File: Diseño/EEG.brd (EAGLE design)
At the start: 49.8 x 80 mm, 42 parts, among them IC1 REF2033AIDDCT, IC2 MCP73831T-2ACI_OT, IC3 LP38692MP-3.3_NOPB, J1 USB3500-30-A-KIT, J2 SJ3-35083A-TR, J3 1769

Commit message: añadido valores cap de carga
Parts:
- C1, C2: value (none) -> 10u
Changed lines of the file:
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@@
 <attribute name="VALUE" x="13.0175" y="34.6075" size="1.27" layer="27" rot="R180" align="center"/>
 </element>
-<element name="C1" library="rcl" library_urn="urn:adsk.eagle:library:334" package="C0805K" package3d_urn="urn:adsk.eagle:package:23681/2" value="" x="22.86" y="22.86" smashed="yes" rot="R180">
+<element name="C1" library="rcl" library_urn="urn:adsk.eagle:library:334" package="C0805K" package3d_urn="urn:adsk.eagle:package:23681/2" value="10u" x="22.86" y="22.86" smashed="yes" rot="R180">
 <attribute name="NAME" x="22.01875" y="20.8775" size="1.016" layer="25"/>
 <attribute name="POPULARITY" value="52" x="-25.4" y="93.98" size="1.778" layer="27" rot="R180" display="off"/>
@@
 <attribute name="VALUE" x="36.195" y="26.67" size="1.27" layer="27" rot="R90"/>
 </element>
-<element name="C2" library="rcl" library_urn="urn:adsk.eagle:library:334" package="C0805K" package3d_urn="urn:adsk.eagle:package:23681/2" value="" x="27.94" y="22.86" smashed="yes">
+<element name="C2" library="rcl" library_urn="urn:adsk.eagle:library:334" package="C0805K" package3d_urn="urn:adsk.eagle:package:23681/2" value="10u" x="27.94" y="22.86" smashed="yes">
 <attribute name="NAME" x="27.09875" y="20.8775" size="1.016" layer="25"/>
 <attribute name="POPULARITY" value="52" x="80.01" y="-48.26" size="1.778" layer="27" display="off"/>

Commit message: Correcciones del profesor
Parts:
- C1, C2: value 10u -> (none)
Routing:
- net +5V: track 72.0 -> 73.4 mm
- net O1: track 51.2 -> 52.5 mm
- net N$10: track 19.8 -> 18.9 mm
- net VSS: track 119.3 -> 120.3 mm
- net CS1: track 27.8 -> 27.2 mm
- net N$15: track 27.6 -> 28.2 mm

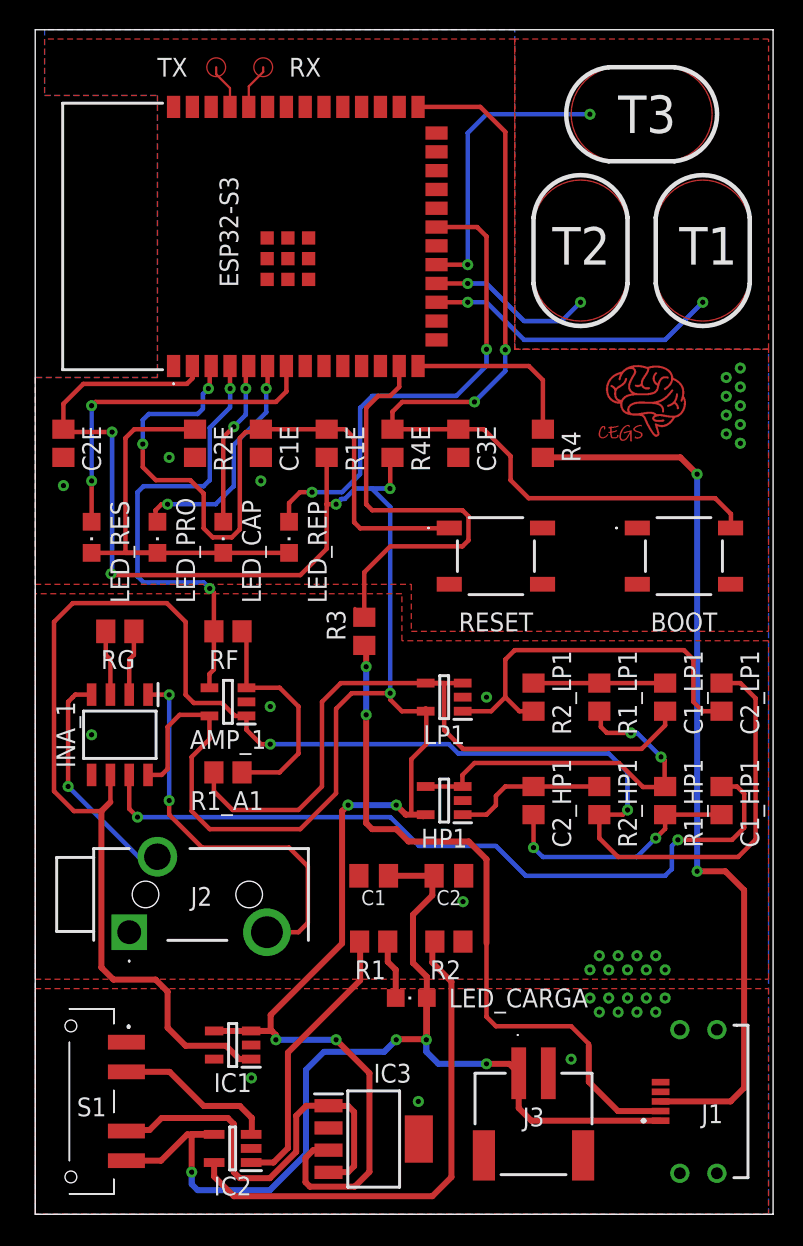
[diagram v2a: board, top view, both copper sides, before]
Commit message: añadido oled, componentes nuevos, restio de leds y correcion de pistas
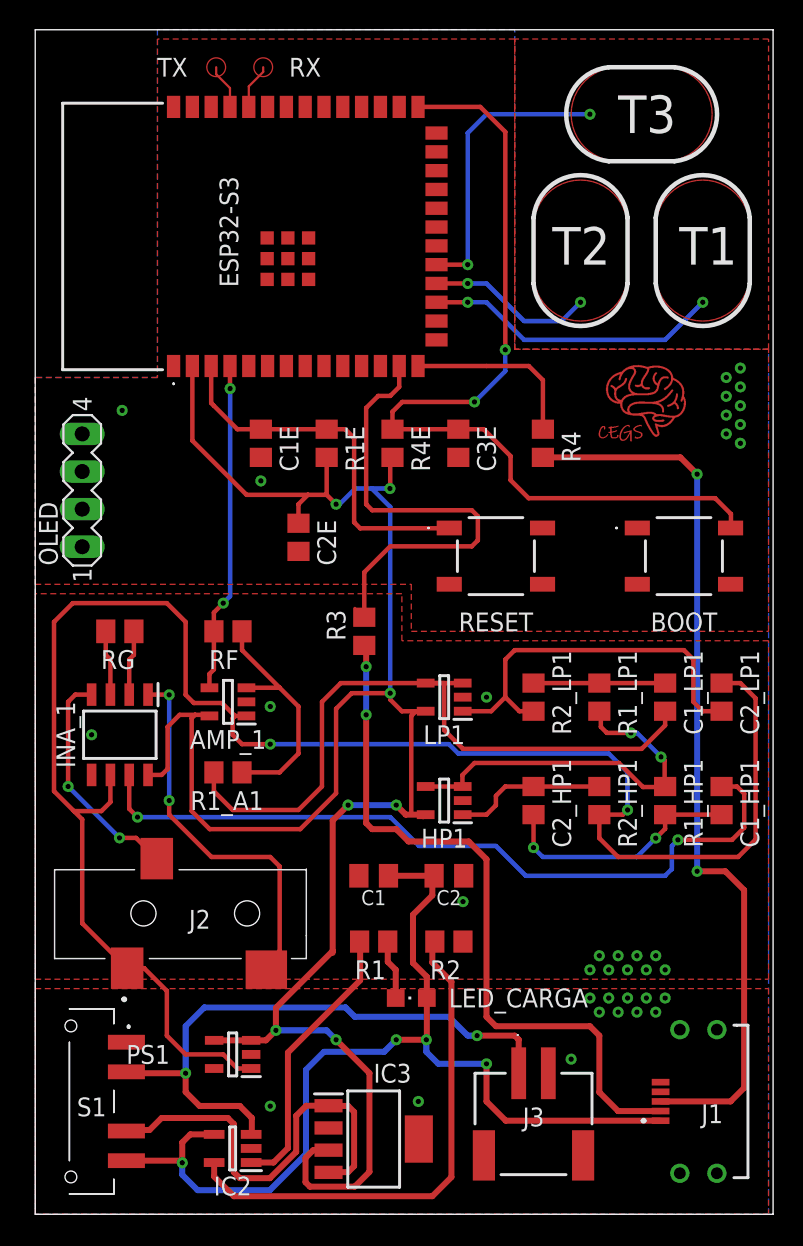
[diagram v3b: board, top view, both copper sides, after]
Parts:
- removed IC1: REF2033AIDDCT, REF2033AIDDCT:SOT95P280X110-5N
- removed LED_CAP, LED_PRO, LED_REP, LED_RES: (no value), led:CHIPLED_0805
- removed R2E: 220, rcl:R0805
- added OLED: (no value), con-lstb:MA04-1
- added PS1: REF2033AIDDCR, REF2033AIDDCR:SOT95P280X110-5N
- J2: value SJ3-35083A-TR -> SJ-3523-SMT-TR; device SJ3-35083A-TR:SJ335083ATR -> SJ-3523-SMT-TR:SJ3523SMTTR
- moved C2E 17.1 mm to (17.8, 45.7)
- moved J2 2.84 mm to (3.81, 20.3)
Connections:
- removed net +5V1: ESP32-S3.22
- removed net LED_REP: ESP32-S3.21, LED_REP.A
- removed net N$1: ESP32-S3.5, LED_CAP.A
- removed net N$15: LED_CAP.C, LED_PRO.C, LED_REP.C, LED_RES.C, R2E.2
- removed net N$16: ESP32-S3.6, LED_PRO.A
- removed net N$17: ESP32-S3.7, LED_RES.A
- new net SCL: ESP32-S3.38, OLED.3
- new net SDA: ESP32-S3.34, OLED.4
- net +3V3: now also OLED.2, PS1.3, PS1.4; no longer IC1.3, IC1.4
- net +5V: no longer J3.1
- net +BATT: now also J3.1
- net CS2: now also J2.3; no longer J2.5
- net GND: now also OLED.1, PS1.2; no longer IC1.2, J2.1, R2E.1
- net VSS: now also J2.1, PS1.1; no longer IC1.1
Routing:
- net LED_REP: track 33.5 -> 0.00 mm, vias 2 -> 0
- net +BATT: track 10.9 -> 41.0 mm, vias 0 -> 2
- net N$15: track 28.2 -> 0.00 mm
- net +3V3: track 167.3 -> 139.4 mm, vias 9 -> 7
- net N$17: track 23.8 -> 0.00 mm, vias 2 -> 0
- net N$19: track 47.5 -> 25.7 mm, vias 2 -> 0
- net N$16: track 16.4 -> 0.00 mm, vias 2 -> 0
- net N$1: track 11.2 -> 0.00 mm, vias 2 -> 0
- net O4: track 32.0 -> 23.0 mm
- net +5V: track 73.4 -> 68.1 mm
- net VSS: track 120.3 -> 121.8 mm
- net CS1: track 27.2 -> 25.8 mm
- net N$18: track 31.5 -> 32.7 mm
- net N$8: track 15.5 -> 16.4 mm
- net USB_2: track 47.8 -> 48.5 mm
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
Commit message: añadí las rutas del nuevo componente
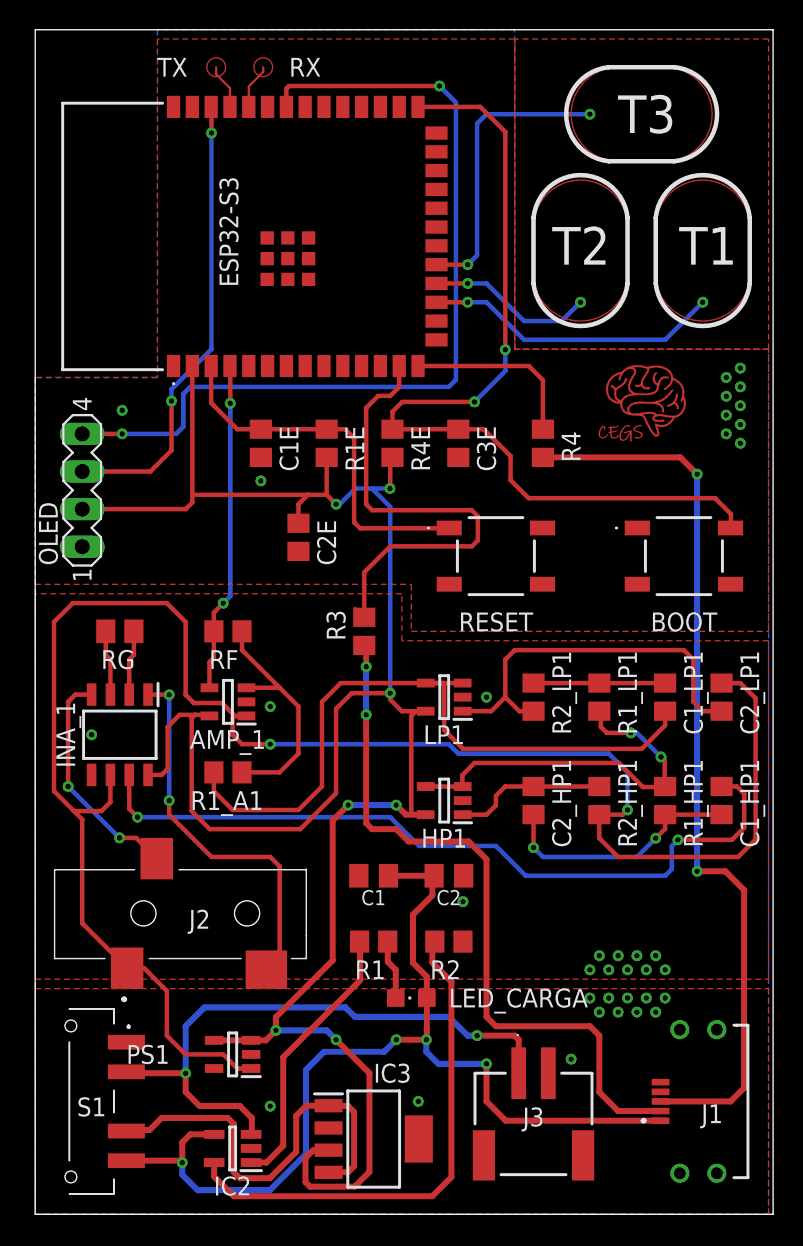
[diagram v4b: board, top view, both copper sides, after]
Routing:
- net SDA: track 0.00 -> 60.0 mm, vias 0 -> 2
- net SCL: track 0.00 -> 30.9 mm, vias 0 -> 2
- net +3V3: track 139.4 -> 149.6 mm
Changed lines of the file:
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@@
 <wire x1="20.32" y1="11.7856" x2="22.57425" y2="9.53135" width="0.4064" layer="1"/>
 <wire x1="22.57425" y1="9.53135" x2="22.57425" y2="2.86098125" width="0.4064" layer="1"/>
-<wire x1="20.0914" y1="17.653" x2="20.0914" y2="17.78" width="0.4064" layer="1"/>
-<wire x1="20.0914" y1="17.78" x2="20.0914" y2="26.5938" width="0.4064" layer="1"/>
+<wire x1="20.0914" y1="17.145" x2="20.0914" y2="26.5938" width="0.4064" layer="1"/>
 <wire x1="20.0914" y1="26.5938" x2="21.1328" y2="27.6352" width="0.4064" layer="1"/>
 <via x="21.1328" y="27.6352" extent="1-16" drill="0.35"/>
@@
 <contactref element="PS1" pad="4"/>
 <wire x1="12.085" y1="11.745" x2="14.585" y2="11.745" width="0.4064" layer="1"/>
-<wire x1="16.256" y1="13.9446" x2="16.256" y2="12.4206" width="0.4064" layer="1"/>
-<wire x1="20.0914" y1="17.78" x2="16.256" y2="13.9446" width="0.4064" layer="1"/>
+<wire x1="16.256" y1="13.3096" x2="16.256" y2="12.4206" width="0.4064" layer="1"/>
+<wire x1="20.0914" y1="17.145" x2="16.256" y2="13.3096" width="0.4064" layer="1"/>
 <wire x1="14.585" y1="11.745" x2="15.5804" y2="11.745" width="0.4064" layer="1"/>
 <wire x1="15.5804" y1="11.745" x2="16.256" y2="12.4206" width="0.4064" layer="1"/>
 <wire x1="19.685" y1="48.5902" x2="20.32" y2="47.9552" width="0.3048" layer="1"/>
-<wire x1="10.615" y1="57.29" x2="10.615" y2="52.25" width="0.3048" layer="1"/>
-<wire x1="14.2748" y1="48.5902" x2="18.415" y2="48.5902" width="0.3048" layer="1"/>
+<wire x1="10.615" y1="57.29" x2="10.615" y2="48.5775" width="0.3048" layer="1"/>
+<wire x1="10.615" y1="48.5775" x2="10.615" y2="48.08" width="0.3048" layer="1"/>
 <wire x1="18.415" y1="48.5902" x2="19.685" y2="48.5902" width="0.3048" layer="1"/>
-<wire x1="10.615" y1="52.25" x2="14.2748" y2="48.5902" width="0.3048" layer="1"/>
 <wire x1="25.4" y1="33.655" x2="25.7175" y2="33.9725" width="0.3048" layer="1"/>
 <wire x1="25.7175" y1="33.9725" x2="25.72" y2="33.975" width="0.3048" layer="1"/>
@@
 <wire x1="17.78" y1="46.67" x2="17.78" y2="47.9552" width="0.3048" layer="1"/>
 <wire x1="17.78" y1="47.9552" x2="18.415" y2="48.5902" width="0.3048" layer="1"/>
-<wire x1="10.795" y1="57.11" x2="3.175" y2="47.625" width="0" layer="19" extent="1-1"/>
+<wire x1="3.175" y1="47.625" x2="10.16" y2="47.625" width="0.3048" layer="1"/>
+<wire x1="10.16" y1="47.625" x2="10.615" y2="48.08" width="0.3048" layer="1"/>
+<wire x1="10.6277" y1="48.5902" x2="10.615" y2="48.5775" width="0.3048" layer="1"/>
+<wire x1="18.415" y1="48.5902" x2="10.6277" y2="48.5902" width="0.3048" layer="1"/>
 </signal>
 <signal name="GND">
@@
 <contactref element="R1" pad="1"/>
 <wire x1="14.585" y1="3.495" x2="14.605" y2="3.475" width="0.1524" layer="1"/>
-<wire x1="14.585" y1="3.495" x2="16.0934" y2="3.495" width="0.4064" layer="1"/>
-<wire x1="17.0688" y1="4.4704" x2="17.0688" y2="10.922" width="0.4064" layer="1"/>
-<wire x1="17.0688" y1="10.922" x2="21.9456" y2="15.7988" width="0.4064" layer="1"/>
+<wire x1="14.585" y1="3.495" x2="15.61715" y2="3.495" width="0.4064" layer="1"/>
+<wire x1="16.7513" y1="4.62915" x2="16.7513" y2="10.6045" width="0.4064" layer="1"/>
+<wire x1="16.7513" y1="10.6045" x2="21.9456" y2="15.7988" width="0.4064" layer="1"/>
 <wire x1="21.9456" y1="15.7988" x2="21.9456" y2="18.3794" width="0.4064" layer="1"/>
 <wire x1="21.9456" y1="18.3794" x2="21.91" y2="18.415" width="0.4064" layer="1"/>
-<wire x1="16.0934" y1="3.495" x2="17.0688" y2="4.4704" width="0.4064" layer="1"/>
+<wire x1="15.61715" y1="3.495" x2="16.7513" y2="4.62915" width="0.4064" layer="1"/>
 </signal>
 <signal name="N$2">
@@
 <contactref element="RF" pad="2"/>
 <contactref element="ESP32-S3" pad="4"/>
-<wire x1="11.7675" y1="36.4925" x2="11.7675" y2="35.5575" width="0.3048" layer="1"/>
-<wire x1="12.0675" y1="36.7925" x2="11.7675" y2="36.4925" width="0.3048" layer="1"/>
-<wire x1="12.0675" y1="39.37" x2="12.0675" y2="36.7925" width="0.3048" layer="1"/>
+<wire x1="11.7675" y1="37.28625" x2="11.7675" y2="35.5575" width="0.3048" layer="1"/>
+<wire x1="12.0675" y1="37.58625" x2="11.7675" y2="37.28625" width="0.3048" layer="1"/>
+<wire x1="12.0675" y1="39.37" x2="12.0675" y2="37.58625" width="0.3048" layer="1"/>
 <wire x1="13.155" y1="57.29" x2="13.155" y2="57.965" width="0.1524" layer="1"/>
 <wire x1="12.065" y1="39.3725" x2="12.0675" y2="39.37" width="0.3048" layer="1"/>
-<wire x1="13.155" y1="57.29" x2="13.155" y2="55.77425" width="0.3048" layer="1"/>
-<wire x1="13.155" y1="55.77425" x2="13.16355" y2="55.7657" width="0.3048" layer="1"/>
-<via x="13.16355" y="55.7657" extent="1-16" drill="0.35"/>
-<wire x1="13.16355" y1="41.73855" x2="12.7" y2="41.275" width="0.3048" layer="16"/>
 <via x="12.7" y="41.275" extent="1-16" drill="0.35"/>
 <wire x1="12.7" y1="41.275" x2="12.065" y2="40.64" width="0.3048" layer="1"/>
 <wire x1="12.065" y1="40.64" x2="12.065" y2="39.3725" width="0.3048" layer="1"/>
-<wire x1="13.16355" y1="55.7657" x2="13.16355" y2="41.73855" width="0.3048" layer="16"/>
+<wire x1="12.7" y1="41.275" x2="13.17625" y2="41.75125" width="0.3048" layer="16"/>
+<via x="13.17625" y="54.76875" extent="1-16" drill="0.35"/>
+<wire x1="13.17625" y1="54.76875" x2="13.17625" y2="57.26875" width="0.3048" layer="1"/>
+<wire x1="13.17625" y1="57.26875" x2="13.155" y2="57.29" width="0.3048" layer="1"/>
+<wire x1="13.17625" y1="41.75125" x2="13.17625" y2="54.76875" width="0.3048" layer="16"/>
 </signal>
 <signal name="CS1">
@@
 <wire x1="27.105" y1="64.135" x2="29.21" y2="64.135" width="0.3048" layer="1"/>
 <via x="29.21" y="64.135" extent="1-16" drill="0.35"/>
-<wire x1="29.21" y1="64.135" x2="29.21" y2="73.025" width="0.3048" layer="16"/>
+<wire x1="29.21" y1="64.135" x2="29.845" y2="64.77" width="0.3048" layer="16"/>
+<wire x1="29.845" y1="73.66" x2="29.845" y2="64.77" width="0.3048" layer="16"/>
 <wire x1="30.48" y1="74.295" x2="37.465" y2="74.295" width="0.3048" layer="16"/>
-<wire x1="30.48" y1="74.295" x2="29.21" y2="73.025" width="0.3048" layer="16"/>
+<wire x1="30.48" y1="74.295" x2="29.845" y2="73.66" width="0.3048" layer="16"/>
 <via x="37.465" y="74.295" extent="1-16" drill="0.35"/>
 </signal>
@@
 <contactref element="OLED" pad="4"/>
 <contactref element="ESP32-S3" pad="34"/>
-<wire x1="3.175" y1="52.705" x2="16.965" y2="74.79" width="0" layer="19" extent="1-1"/>
+<wire x1="16.965" y1="74.79" x2="16.965" y2="76.02" width="0.3048" layer="1"/>
+<wire x1="16.965" y1="76.02" x2="17.145" y2="76.2" width="0.3048" layer="1"/>
+<wire x1="17.145" y1="76.2" x2="27.305" y2="76.2" width="0.3048" layer="1"/>
+<via x="27.305" y="76.2" extent="1-16" drill="0.35"/>
+<wire x1="27.305" y1="76.2" x2="28.41625" y2="75.08875" width="0.3048" layer="16"/>
+<wire x1="28.41625" y1="56.35625" x2="27.94" y2="55.88" width="0.3048" layer="16"/>
+<wire x1="28.41625" y1="75.08875" x2="28.41625" y2="56.35625" width="0.3048" layer="16"/>
+<wire x1="27.94" y1="55.88" x2="10.4775" y2="55.88" width="0.3048" layer="16"/>
+<wire x1="10.4775" y1="55.88" x2="10.00125" y2="55.40375" width="0.3048" layer="16"/>
+<wire x1="10.00125" y1="55.40375" x2="10.00125" y2="53.18125" width="0.3048" layer="16"/>
+<wire x1="10.00125" y1="53.18125" x2="9.525" y2="52.705" width="0.3048" layer="16"/>
+<wire x1="9.525" y1="52.705" x2="5.87375" y2="52.705" width="0.3048" layer="16"/>
+<via x="5.87375" y="52.705" extent="1-16" drill="0.35"/>
+<wire x1="5.87375" y1="52.705" x2="3.175" y2="52.705" width="0.3048" layer="1"/>
 </signal>
 <signal name="SCL">
 <contactref element="OLED" pad="3"/>
 <contactref element="ESP32-S3" pad="38"/>
-<wire x1="3.175" y1="50.165" x2="11.885" y2="74.79" width="0" layer="19" extent="1-1"/>
+<wire x1="3.175" y1="50.165" x2="7.77875" y2="50.165" width="0.3048" layer="1"/>
+<wire x1="11.90625" y1="73.025" x2="11.90625" y2="58.42" width="0.3048" layer="16"/>
+<via x="11.90625" y="73.025" extent="1-16" drill="0.35"/>
+<wire x1="11.90625" y1="73.025" x2="11.90625" y2="74.76875" width="0.3048" layer="1"/>
+<wire x1="11.90625" y1="74.76875" x2="11.885" y2="74.79" width="0.3048" layer="1"/>
+<wire x1="9.2075" y1="51.59375" x2="7.77875" y2="50.165" width="0.3048" layer="1"/>
+<wire x1="9.2075" y1="55.72125" x2="9.2075" y2="54.9275" width="0.3048" layer="16"/>
+<via x="9.2075" y="54.9275" extent="1-16" drill="0.35"/>
+<wire x1="11.90625" y1="58.42" x2="9.2075" y2="55.72125" width="0.3048" layer="16"/>
+<wire x1="9.2075" y1="54.9275" x2="9.2075" y2="51.59375" width="0.3048" layer="1"/>
 </signal>
 </signals>

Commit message: por fin acabamos esto
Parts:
- C1, C2: value (none) -> 10u
- moved OLED 0.63 mm to (3.17, 49.5), turned to 270 degrees
- renumbered AMP_1 to AMP, C1E to C7, C1_HP1 to C3, C1_LP1 to C6, C2E to C8, C2_HP1 to C4, C2_LP1 to C5, C3E to C9, HP1 to HP, INA_1 to INA, LED_CARGA to LED, LP1 to LP, R1E to R11, R1_A1 to R9, R1_HP1 to R6, R1_LP1 to R7, R2_HP1 to R5, R2_LP1 to R8, R4E to R12, RF to R10
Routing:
- net +3V3: track 149.6 -> 130.7 mm
- net N$18: track 32.7 -> 18.4 mm, vias 0 -> 2
- net SDA: track 60.0 -> 67.0 mm, vias 2 -> 1
- net USB_3: track 60.8 -> 66.9 mm
- net TOUCHP_2: track 11.3 -> 15.3 mm
- net TOUCHP_1: track 20.1 -> 24.0 mm
- net N$8: track 16.4 -> 19.0 mm
- net SCL: track 30.9 -> 32.4 mm, vias 2 -> 1
- net +BATT: track 41.0 -> 39.9 mm
- net O4: track 23.0 -> 22.3 mm
- net N$11: track 29.1 -> 28.5 mm
